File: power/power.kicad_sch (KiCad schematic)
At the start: 17 parts, among them J1 GPIO, J18 JP_VCC_PWM, J19 Conn_01x01, J2 PWM_OUT, J3 PWM_IN, J4 JP_EXT, J5 JP_VOLTS, J8 PWM_OUT, J9 JP_VCC_PWM, Q1 D15P05

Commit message: change footprints; fix ERC unconnected signals
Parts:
- J19: now left out of the parts list
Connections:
- no-connect marks 22 -> 25
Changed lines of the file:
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@@
 	)
 	(no_connect
+		(at 60.96 49.53)
+	)
+	(no_connect
+		(at 73.66 44.45)
+	)
+	(no_connect
 		(at 73.66 49.53)
 	)
 	(no_connect
+		(at 73.66 46.99)
+	)
+	(no_connect
 		(at 60.96 77.47)
 	)
@@
 		(body_style 1)
 		(exclude_from_sim no)
-		(in_bom yes)
+		(in_bom no)
 		(on_board yes)
 		(in_pos_files yes)

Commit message: connect unused RPi pins; use 12 pin not 16 pin header; make pinheaders/-sockets DNP
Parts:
- J1, J2, J3, J5, J8: now not fitted
- J4: footprint Connector_PinHeader_2.54mm:PinHeader_2x08_P2.54mm_Vertical -> Connector_PinHeader_2.54mm:PinHeader_2x06_P2.54mm_Vertical; symbol Connector_Generic:Conn_02x08_Odd_Even -> Connector_Generic:Conn_02x06_Odd_Even; Part PZ254R-12-16P -> 2541WR-2x06P; now not fitted
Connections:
- net GND: now also J4.11 (Pin_11), J4.12 (Pin_12); no longer J4.16 (Pin_16)
- net GPIO13/PWM1: now also J4.7 (Pin_7)
- net GPIO16: now also J4.10 (Pin_10)
- net GPIO22: now also J4.6 (Pin_6)
- net GPIO23: now also J4.3 (Pin_3)
- net GPIO24: now also J4.5 (Pin_5)
- net GPIO26: now also J4.9 (Pin_9)
- net GPIO27: now also J4.4 (Pin_4)
- net GPIO5: now also J4.8 (Pin_8)

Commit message: don't use DNP
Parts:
- J1, J18, J2, J3, J4, J5, J8, J9: now fitted
- JP1: Part 2541WV-2X01P -> (none)
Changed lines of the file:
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@@
 		(on_board yes)
 		(in_pos_files no)
-		(dnp yes)
+		(dnp no)
 		(property "Reference" "J1"
 			(at 67.31 31.3498 0)
@@
 		(on_board yes)
 		(in_pos_files no)
-		(dnp yes)
+		(dnp no)
 		(fields_autoplaced yes)
 		(property "Reference" "J8"
@@
 			)
 		)
-		(property "Part" "2541WV-2X01P"
+		(property "Part" ""
 			(at 250.19 154.94 0)
 			(hide yes)
@@
 		(on_board yes)
 		(in_pos_files no)
-		(dnp yes)
+		(dnp no)
 		(fields_autoplaced yes)
 		(property "Reference" "J2"
@@
 		(on_board yes)
 		(in_pos_files no)
-		(dnp yes)
+		(dnp no)
 		(property "Reference" "J5"
 			(at 133.096 27.94 0)
@@
 		(on_board yes)
 		(in_pos_files yes)
-		(dnp yes)
+		(dnp no)
 		(property "Reference" "J18"
 			(at 348.996 90.932 0)
@@
 		(on_board yes)
 		(in_pos_files no)
-		(dnp yes)
+		(dnp no)
 		(property "Reference" "J3"
 			(at 346.71 46.9899 0)
@@
 		(on_board yes)
 		(in_pos_files no)
-		(dnp yes)
+		(dnp no)
 		(fields_autoplaced yes)
 		(property "Reference" "J4"
@@
 		(on_board yes)
 		(in_pos_files yes)
-		(dnp yes)
+		(dnp no)
 		(property "Reference" "J9"
 			(at 349.504 82.042 0)

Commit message: exclude solderjumper from BOM
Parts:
- JP1: now left out of the parts list
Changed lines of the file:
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@@
 		(body_style 1)
 		(exclude_from_sim no)
-		(in_bom yes)
+		(in_bom no)
 		(on_board yes)
-		(in_pos_files yes)
+		(in_pos_files no)
 		(dnp no)
 		(fields_autoplaced yes)

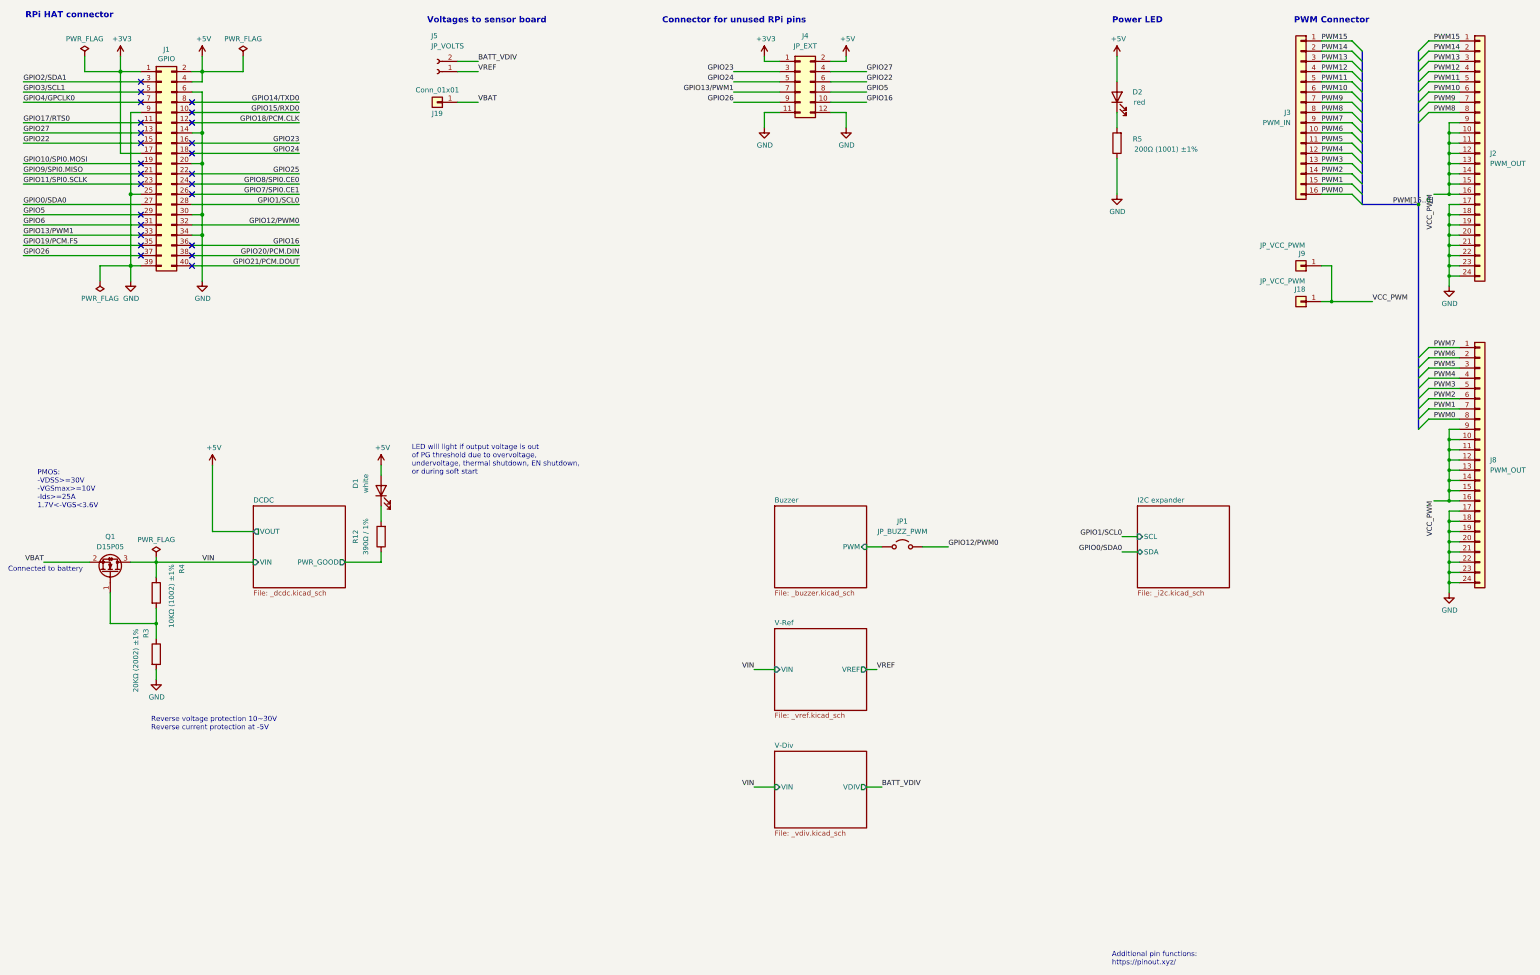
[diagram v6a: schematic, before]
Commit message: added RGB indicator LED w/LP5562; added I2C pullups
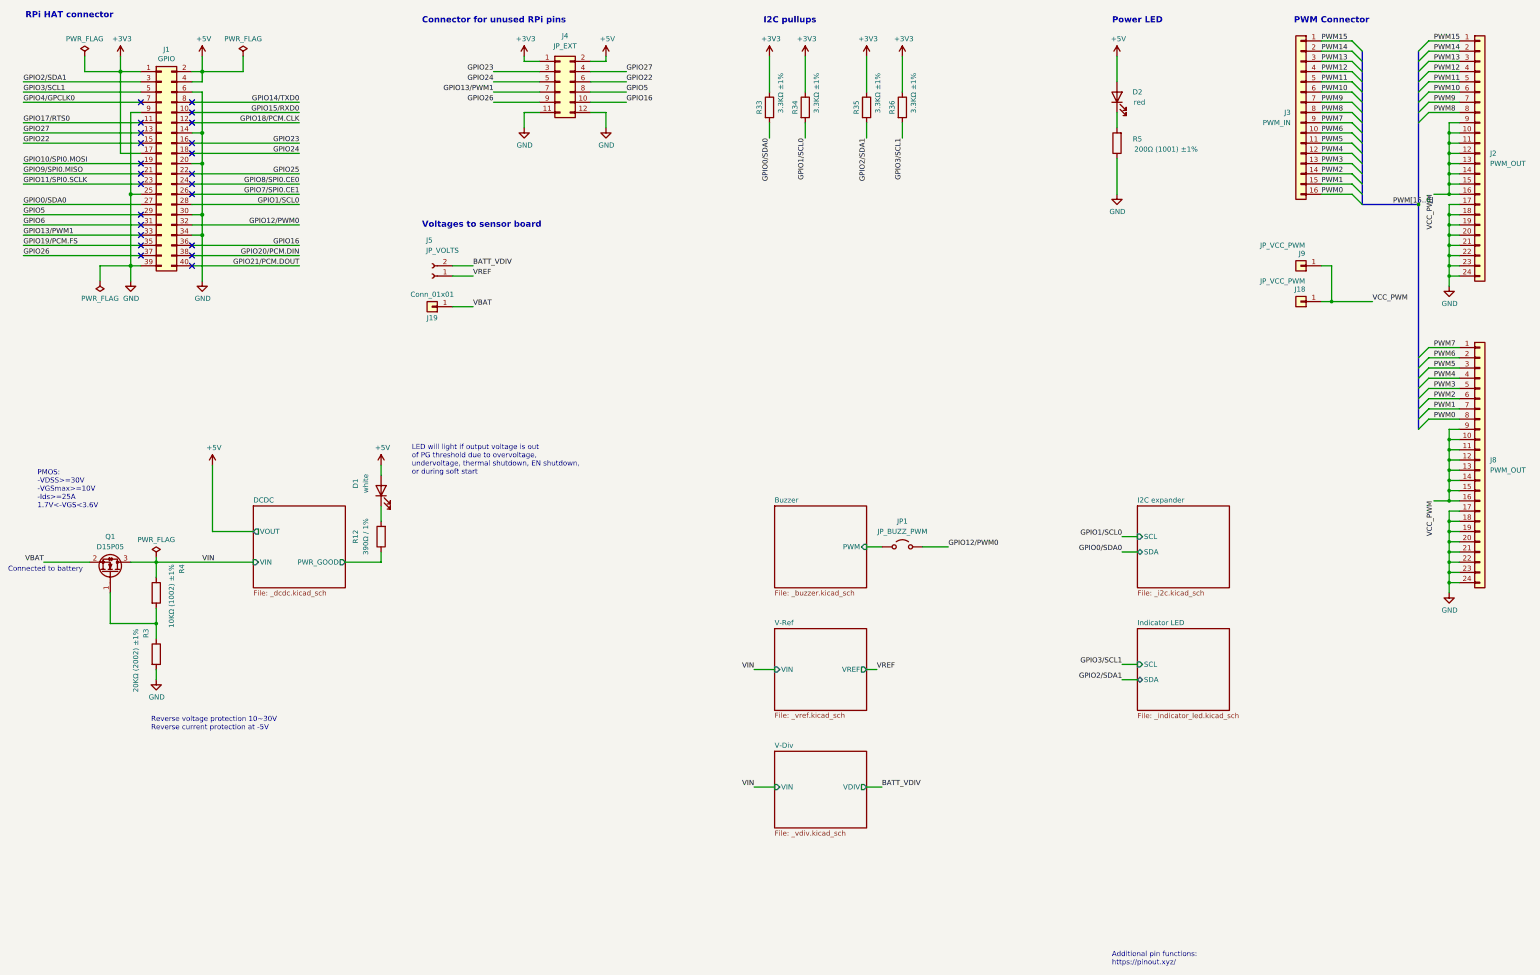
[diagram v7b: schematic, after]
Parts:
- added R33, R34, R35, R36: 3.3KΩ ±1%, Resistor_SMD:R_0402_1005Metric, symbol Device:R
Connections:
- net +3V3: now also R33.1, R34.1, R35.1, R36.1
- net GPIO0/SDA0: now also R33.2
- net GPIO1/SCL0: now also R34.2
- net GPIO2/SDA1: now also R35.2
- net GPIO3/SCL1: now also R36.2
- no-connect marks 25 -> 23
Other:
- added sheet Indicator LED (_indicator_led.kicad_sch)
- note added: "I2C pullups"
- moved on the sheet: J19, J4, J5

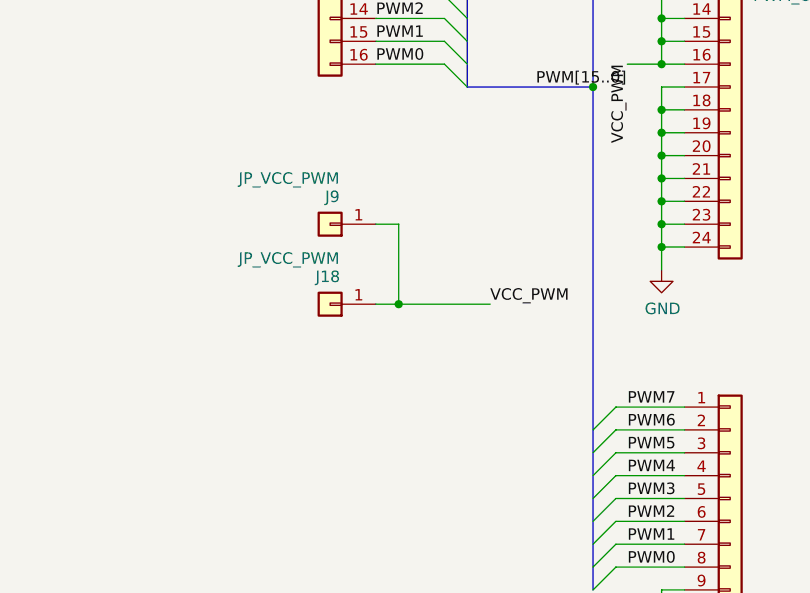
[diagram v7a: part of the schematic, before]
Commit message: add 5V pin pad near PWM VCC input pin
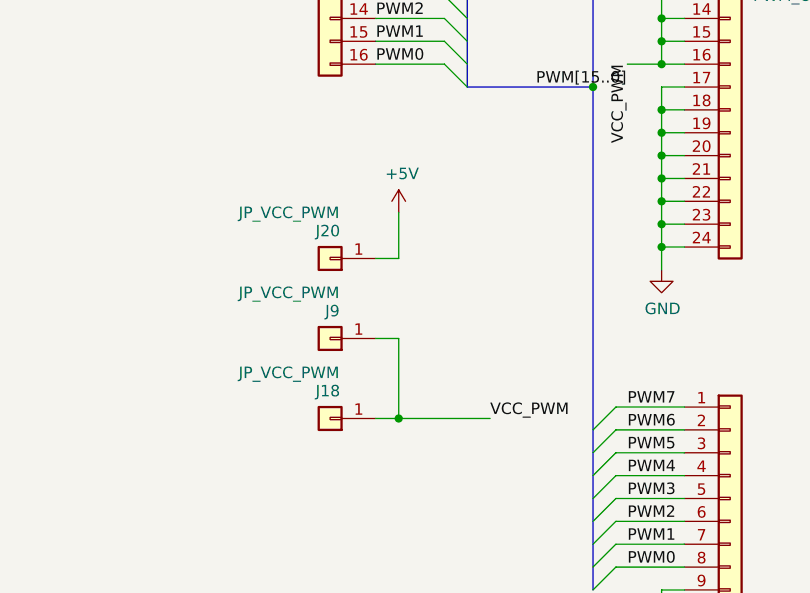
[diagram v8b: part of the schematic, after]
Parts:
- added J20: JP_VCC_PWM, Connector_PinHeader_2.54mm:PinHeader_1x01_P2.54mm_Vertical, symbol Connector_Generic:Conn_01x01
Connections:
- net +5V: now also J20.1 (Pin_1)
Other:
- moved on the sheet: J18, J9
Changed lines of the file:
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@@
 	)
 	(junction
-		(at 356.87 93.98)
+		(at 356.87 106.68)
 		(diameter 0)
 		(color 0 0 0 0)
@@
 	(wire
 		(pts
+			(xy 356.87 88.9) (xy 356.87 83.82)
+		)
+		(stroke
+			(width 0)
+			(type default)
+		)
+	)
+	(wire
+		(pts
 			(xy 386.08 161.29) (xy 388.62 161.29)
 		)
@@
 	(wire
 		(pts
-			(xy 356.87 93.98) (xy 354.33 93.98)
+			(xy 356.87 106.68) (xy 354.33 106.68)
 		)
 		(stroke
@@
 	(wire
 		(pts
-			(xy 354.33 85.09) (xy 356.87 85.09)
+			(xy 354.33 97.79) (xy 356.87 97.79)
 		)
 		(stroke
@@
 	(wire
 		(pts
-			(xy 356.87 85.09) (xy 356.87 93.98)
+			(xy 356.87 97.79) (xy 356.87 106.68)
 		)
 		(stroke
@@
 	(wire
 		(pts
+			(xy 354.33 88.9) (xy 356.87 88.9)
+		)
+		(stroke
+			(width 0)
+			(type default)
+		)
+	)
+	(wire
+		(pts
 			(xy 386.08 130.81) (xy 386.08 133.35)
 		)
@@
 	(wire
 		(pts
-			(xy 356.87 93.98) (xy 367.03 93.98)
+			(xy 356.87 106.68) (xy 367.03 106.68)
 		)
 		(stroke
@@
 	)
 	(label "VCC_PWM"
-		(at 367.03 93.98 0)
+		(at 367.03 106.68 0)
 		(effects
 			(font
@@
 	)
 	(symbol
+		(lib_id "Connector_Generic:Conn_01x01")
+		(at 349.25 88.9 180)
+		(unit 1)
+		(body_style 1)
+		(exclude_from_sim no)
+		(in_bom no)
+		(on_board yes)
+		(in_pos_files no)
+		(dnp no)
+		(property "Reference" "J20"
+			(at 348.996 85.852 0)
+			(show_name no)
+			(do_not_autoplace no)
+			(effects
+				(font
+					(size 1.27 1.27)
+				)
+			)
+		)
+		(property "Value" "JP_VCC_PWM"
+			(at 344.678 83.82 0)
+			(show_name no)
+			(do_not_autoplace no)
+			(effects
+				(font
+					(size 1.27 1.27)
+				)
+			)
+		)
+		(property "Footprint" "Connector_PinHeader_2.54mm:PinHeader_1x01_P2.54mm_Vertical"
+			(at 349.25 88.9 0)
+			(hide yes)
+			(show_name no)
+			(do_not_autoplace no)
+			(effects
+				(font
+					(size 1.27 1.27)
+				)
+			)
+		)
+		(property "Datasheet" ""
+			(at 349.25 88.9 0)
+			(hide yes)
+			(show_name no)
+			(do_not_autoplace no)
+			(effects
+				(font
+					(size 1.27 1.27)
+				)
+			)
+		)
+		(property "Description" "Generic connector, single row, 01x01, script generated (kicad-library-utils/schlib/autogen/connector/)"
+			(at 349.25 88.9 0)
+			(hide yes)
+			(show_name no)
+			(do_not_autoplace no)
+			(effects
+				(font
+					(size 1.27 1.27)
+				)
+			)
+		)
+		(property "Part" ""
+			(at 349.25 88.9 0)
+			(hide yes)
+			(show_name no)
+			(do_not_autoplace no)
+			(effects
+				(font
+					(size 1.27 1.27)
+				)
+			)
+		)
+		(pin "1"
+		)
+		(instances
+			(project "power"
+				(path "/e63e39d7-6ac0-4ffd-8aa3-1841a4541b55"
+					(reference "J20")
+					(unit 1)
+				)
+			)
+		)
+	)
+	(symbol
 		(lib_id "power:GND")
 		(at 303.53 67.31 0)
@@
 	)
 	(symbol
+		(lib_id "power:+5V")
+		(at 356.87 83.82 0)
+		(unit 1)
+		(body_style 1)
+		(exclude_from_sim no)
+		(in_bom yes)
+		(on_board yes)
+		(in_pos_files yes)
+		(dnp no)
+		(property "Reference" "#PWR022"
+			(at 356.87 87.63 0)
+			(hide yes)
+			(show_name no)
+			(do_not_autoplace no)
+			(effects
+				(font
+					(size 1.27 1.27)
+				)
+			)
+		)
+		(property "Value" "+5V"
+			(at 357.2383 79.4956 0)
+			(show_name no)
+			(do_not_autoplace no)
+			(effects
+				(font
+					(size 1.27 1.27)
+				)
+			)
+		)
+		(property "Footprint" ""
+			(at 356.87 83.82 0)
+			(show_name no)
+			(do_not_autoplace no)
+			(effects
+				(font
+					(size 1.27 1.27)
+				)
+			)
+		)
+		(property "Datasheet" ""
+			(at 356.87 83.82 0)
+			(show_name no)
+			(do_not_autoplace no)
+			(effects
+				(font
+					(size 1.27 1.27)
+				)
+			)
+		)
+		(property "Description" "Power symbol creates a global label with name \"+5V\""
+			(at 356.87 83.82 0)
+			(hide yes)
+			(show_name no)
+			(do_not_autoplace no)
+			(effects
+				(font
+					(size 1.27 1.27)
+				)
+			)
+		)
+		(pin "1"
+		)
+		(instances
+			(project "power"
+				(path "/e63e39d7-6ac0-4ffd-8aa3-1841a4541b55"
+					(reference "#PWR022")
+					(unit 1)
+				)
+			)
+		)
+	)
+	(symbol
 		(lib_id "Device:LED")
 		(at 120.65 140.97 90)
@@
 	(symbol
 		(lib_id "Connector_Generic:Conn_01x01")
-		(at 349.25 93.98 180)
+		(at 349.25 106.68 180)
 		(unit 1)
 		(body_style 1)
@@
 		(dnp no)
 		(property "Reference" "J18"
-			(at 348.996 90.932 0)
+			(at 348.996 103.632 0)
 			(show_name no)
 			(do_not_autoplace no)
@@
 		)
 		(property "Value" "JP_VCC_PWM"
-			(at 344.678 88.9 0)
+			(at 344.678 101.6 0)
 			(show_name no)
 			(do_not_autoplace no)
@@
 		)
 		(property "Footprint" "Connector_PinHeader_2.54mm:PinHeader_1x01_P2.54mm_Vertical"
-			(at 349.25 93.98 0)
+			(at 349.25 106.68 0)
 			(hide yes)
 			(show_name no)
@@
 		)
 		(property "Datasheet" ""
-			(at 349.25 93.98 0)
+			(at 349.25 106.68 0)
 			(hide yes)
 			(show_name no)
@@
 		)
 		(property "Description" "Generic connector, single row, 01x01, script generated (kicad-library-utils/schlib/autogen/connector/)"
-			(at 349.25 93.98 0)
+			(at 349.25 106.68 0)
 			(hide yes)
 			(show_name no)
@@
 		)
 		(property "Part" ""
-			(at 349.25 93.98 0)
+			(at 349.25 106.68 0)
 			(hide yes)
 			(show_name no)
@@
 	(symbol
 		(lib_id "Connector_Generic:Conn_01x01")
-		(at 349.25 85.09 180)
+		(at 349.25 97.79 180)
 		(unit 1)
 		(body_style 1)
@@
 		(dnp no)
 		(property "Reference" "J9"
-			(at 349.504 82.042 0)
+			(at 349.504 94.742 0)
 			(show_name no)
 			(do_not_autoplace no)
@@
 		)
 		(property "Value" "JP_VCC_PWM"
-			(at 344.678 80.01 0)
+			(at 344.678 92.71 0)
 			(show_name no)
 			(do_not_autoplace no)
@@
 		)
 		(property "Footprint" "Connector_PinHeader_2.54mm:PinHeader_1x01_P2.54mm_Vertical"
-			(at 349.25 85.09 0)
+			(at 349.25 97.79 0)
 			(hide yes)
 			(show_name no)
@@
 		)
 		(property "Datasheet" ""
-			(at 349.25 85.09 0)
+			(at 349.25 97.79 0)
 			(hide yes)
 			(show_name no)
@@
 		)
 		(property "Description" "Generic connector, single row, 01x01, script generated (kicad-library-utils/schlib/autogen/connector/)"
-			(at 349.25 85.09 0)
+			(at 349.25 97.79 0)
 			(hide yes)
 			(show_name no)
@@
 		)
 		(property "Part" ""
-			(at 349.25 85.09 0)
+			(at 349.25 97.79 0)
 			(hide yes)
 			(show_name no)
